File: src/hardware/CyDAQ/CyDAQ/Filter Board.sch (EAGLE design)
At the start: 213 parts, among them J1 DCJ0202, J10 Vout_HEADER, J11 5V0_SENSOR, J12 3V3_SENSOR, J13 1V8_SENSOR, J14 BRKOUT_JD, J15 BRKOUT_JC, J16 BRKOUT_JB, J17 BRKOUT_JF, J18 5V0_CONN, J19 3V3_CONN, J2 ZYBO_JF, J20 1V8_CONN, J21 BRKOUT_JD, J22 ZYBO_Power, J3 ZYBO_JE, J4 ZYBO_JD, J5 ZYBO_JC, J6 ZYBO_JB, J7 A_XADC, J8 SJ1-3523N, J9 Vin_HEADER, U1 TPS54531DDARDDA8_3P1X2P4-L, U10 CD74HCT4051, U11 CD74HCT4051, U12 OPA4197, U13 OPA4197, U14 OPA4197, U15 OPA4197, U16 OPA4197, U17 CD74HCT4053, U18 CD74HCT4051, U19 OPA2197, U3 TPS56339, U4 TPS56339, U5 LM43601PWPR, U6 X9258_A, U7 X925_B, U8 X9258_C, U9 X9258_D

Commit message: Made some final adjustments and added production files
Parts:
- added R43: 10k, Resistors:SMD_0805
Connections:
- net 3.5MM_IN: now also J8.2; no longer J8.1
- net GND: now also J8.1, R43.1; no longer J8.2
- net N$73: now also R43.2
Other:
- note removed: "Pull-up/down resistors on U1"
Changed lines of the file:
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@@
 <attribute name="ENGINEER_NAME" value="Samuel Burnett"/>
 </part>
+<part name="R43" library="Resistors" library_urn="urn:adsk.eagle:library:4010572" deviceset="SMD" device="_0805" package3d_urn="urn:adsk.eagle:package:4010580/4" value="10k"/>
+<part name="SUPPLY93" library="supply2" library_urn="urn:adsk.eagle:library:372" deviceset="GND" device=""/>
 </parts>
 <sheets>
@@
 <text x="195.072" y="108.712" size="1.27" layer="97">NC</text>
 <text x="324.612" y="108.712" size="1.27" layer="97">NC</text>
-<text x="10.16" y="40.132" size="1.778" layer="97">Pull-up/down
-resistors on U1</text>
-<text x="294.64" y="114.3" size="1.778" layer="97">Pull-up/down
-resistors on U1</text>
-<text x="170.18" y="114.3" size="1.778" layer="97">Pull-up/down
-resistors on U1</text>
 <text x="93.726" y="128.524" size="1.778" layer="97">Address: 0x0</text>
 <text x="218.186" y="128.524" size="1.778" layer="97">Address: 0x6</text>
@@
 <text x="229.108" y="73.152" size="1.27" layer="97">0.1%</text>
 <text x="244.094" y="73.152" size="1.27" layer="97">0.1%</text>
-<wire x1="152.4" y1="88.9" x2="271.78" y2="88.9" width="0.1524" layer="97" style="longdash"/>
-<wire x1="271.78" y1="88.9" x2="271.78" y2="10.16" width="0.1524" layer="97" style="longdash"/>
-<wire x1="271.78" y1="10.16" x2="152.4" y2="10.16" width="0.1524" layer="97" style="longdash"/>
+<wire x1="152.4" y1="88.9" x2="276.86" y2="88.9" width="0.1524" layer="97" style="longdash"/>
+<wire x1="276.86" y1="88.9" x2="276.86" y2="10.16" width="0.1524" layer="97" style="longdash"/>
+<wire x1="276.86" y1="10.16" x2="152.4" y2="10.16" width="0.1524" layer="97" style="longdash"/>
 <wire x1="152.4" y1="10.16" x2="152.4" y2="88.9" width="0.1524" layer="97" style="longdash"/>
 <text x="154.94" y="71.12" size="5.08" layer="97">Level shifter</text>
@@
 <attribute name="VALUE" x="25.3947" y="128.7727" size="1.778" layer="96"/>
 </instance>
-<instance part="SUPPLY74" gate="GND" x="48.26" y="129.54" smashed="yes"/>
+<instance part="SUPPLY74" gate="GND" x="68.58" y="134.62" smashed="yes"/>
 <instance part="J9" gate="G$1" x="27.94" y="33.02" smashed="yes">
 <attribute name="VALUE" x="25.4" y="28.194" size="1.778" layer="96" font="vector"/>
@@
 <attribute name="ENGINEER_NAME" x="346.71" y="19.05" size="2.54" layer="94"/>
 </instance>
+<instance part="R43" gate="G$1" x="271.78" y="55.88" smashed="yes" rot="R90">
+<attribute name="NAME" x="270.8656" y="60.579" size="1.778" layer="95" rot="R180"/>
+<attribute name="VALUE" x="270.891" y="52.197" size="1.778" layer="96" rot="R180"/>
+</instance>
+<instance part="SUPPLY93" gate="GND" x="271.78" y="45.72" smashed="yes"/>
 </instances>
 <busses>
@@
 </segment>
 <segment>
-<pinref part="J8" gate="G$1" pin="2"/>
-<wire x1="43.18" y1="134.62" x2="48.26" y2="134.62" width="0.1524" layer="91"/>
-<wire x1="48.26" y1="134.62" x2="48.26" y2="132.08" width="0.1524" layer="91"/>
-<pinref part="SUPPLY74" gate="GND" pin="GND"/>
-</segment>
-<segment>
 <pinref part="J9" gate="G$1" pin="1"/>
 <wire x1="35.56" y1="33.02" x2="43.18" y2="33.02" width="0.1524" layer="91"/>
@@
 <pinref part="SUPPLY9" gate="GND" pin="GND"/>
 </segment>
+<segment>
+<pinref part="J8" gate="G$1" pin="1"/>
+<pinref part="SUPPLY74" gate="GND" pin="GND"/>
+<wire x1="43.18" y1="139.7" x2="68.58" y2="139.7" width="0.1524" layer="91"/>
+<wire x1="68.58" y1="139.7" x2="68.58" y2="137.16" width="0.1524" layer="91"/>
+</segment>
+<segment>
+<pinref part="R43" gate="G$1" pin="1"/>
+<pinref part="SUPPLY93" gate="GND" pin="GND"/>
+<wire x1="271.78" y1="50.8" x2="271.78" y2="48.26" width="0.1524" layer="91"/>
+</segment>
 </net>
 <net name="3.5MM_IN" class="0">
 <segment>
-<pinref part="J8" gate="G$1" pin="1"/>
-<wire x1="43.18" y1="139.7" x2="48.26" y2="139.7" width="0.1524" layer="91"/>
-<label x="62.738" y="139.7" size="1.27" layer="95" rot="R180" xref="yes"/>
+<pinref part="J8" gate="G$1" pin="2"/>
+<wire x1="43.18" y1="134.62" x2="48.26" y2="134.62" width="0.1524" layer="91"/>
+<label x="62.738" y="134.62" size="1.27" layer="95" rot="R180" xref="yes"/>
 </segment>
 </net>
@@
 <wire x1="299.72" y1="73.66" x2="302.26" y2="73.66" width="0.1524" layer="91"/>
 <wire x1="302.26" y1="73.66" x2="302.26" y2="66.04" width="0.1524" layer="91"/>
-<wire x1="302.26" y1="66.04" x2="264.16" y2="66.04" width="0.1524" layer="91"/>
+<wire x1="302.26" y1="66.04" x2="271.78" y2="66.04" width="0.1524" layer="91"/>
 <junction x="264.16" y="66.04"/>
+<pinref part="R43" gate="G$1" pin="2"/>
+<wire x1="271.78" y1="66.04" x2="264.16" y2="66.04" width="0.1524" layer="91"/>
+<wire x1="271.78" y1="60.96" x2="271.78" y2="66.04" width="0.1524" layer="91"/>
+<junction x="271.78" y="66.04"/>
 </segment>
 </net>

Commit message: Adjusted notch filter values and uploaded BOM
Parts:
- C31: value 10uF -> 0.1uF
- C34, C35: value 5.6uF -> 0.1uF
- R39, R40: value 470 -> 39k
- R46: value 220 -> 9.1k
- R60, R65: value 50k -> 51k
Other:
- note added: "Center Frequency = 59Hz"
- note removed: "Center Frequency = 64Hz"
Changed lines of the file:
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@@
 <part name="U10" library="Digital ICs" library_urn="urn:adsk.eagle:library:14993291" deviceset="CD74HCT4051" device="" package3d_urn="urn:adsk.eagle:package:14993294/2" value="CD74HCT4051"/>
 <part name="U11" library="Digital ICs" library_urn="urn:adsk.eagle:library:14993291" deviceset="CD74HCT4051" device="" package3d_urn="urn:adsk.eagle:package:14993294/2" value="CD74HCT4051"/>
-<part name="R39" library="Resistors" library_urn="urn:adsk.eagle:library:4010572" deviceset="SMD" device="_0805" package3d_urn="urn:adsk.eagle:package:4010580/4" value="470"/>
-<part name="R40" library="Resistors" library_urn="urn:adsk.eagle:library:4010572" deviceset="SMD" device="_0805" package3d_urn="urn:adsk.eagle:package:4010580/4" value="470"/>
-<part name="R46" library="Resistors" library_urn="urn:adsk.eagle:library:4010572" deviceset="SMD" device="_0805" package3d_urn="urn:adsk.eagle:package:4010580/4" value="220"/>
-<part name="C35" library="Capacitors" library_urn="urn:adsk.eagle:library:4010381" deviceset="NON_POL" device="_0805/2012" package3d_urn="urn:adsk.eagle:package:4010399/3" value="5.6uF"/>
-<part name="C34" library="Capacitors" library_urn="urn:adsk.eagle:library:4010381" deviceset="NON_POL" device="_0805/2012" package3d_urn="urn:adsk.eagle:package:4010399/3" value="5.6uF"/>
-<part name="C31" library="Capacitors" library_urn="urn:adsk.eagle:library:4010381" deviceset="NON_POL" device="_0805/2012" package3d_urn="urn:adsk.eagle:package:4010399/3" value="10uF"/>
+<part name="R39" library="Resistors" library_urn="urn:adsk.eagle:library:4010572" deviceset="SMD" device="_0805" package3d_urn="urn:adsk.eagle:package:4010580/4" value="39k"/>
+<part name="R40" library="Resistors" library_urn="urn:adsk.eagle:library:4010572" deviceset="SMD" device="_0805" package3d_urn="urn:adsk.eagle:package:4010580/4" value="39k"/>
+<part name="R46" library="Resistors" library_urn="urn:adsk.eagle:library:4010572" deviceset="SMD" device="_0805" package3d_urn="urn:adsk.eagle:package:4010580/4" value="9.1k"/>
+<part name="C35" library="Capacitors" library_urn="urn:adsk.eagle:library:4010381" deviceset="NON_POL" device="_0805/2012" package3d_urn="urn:adsk.eagle:package:4010399/3" value="0.1uF"/>
+<part name="C34" library="Capacitors" library_urn="urn:adsk.eagle:library:4010381" deviceset="NON_POL" device="_0805/2012" package3d_urn="urn:adsk.eagle:package:4010399/3" value="0.1uF"/>
+<part name="C31" library="Capacitors" library_urn="urn:adsk.eagle:library:4010381" deviceset="NON_POL" device="_0805/2012" package3d_urn="urn:adsk.eagle:package:4010399/3" value="0.1uF"/>
 <part name="SUPPLY44" library="supply2" library_urn="urn:adsk.eagle:library:372" deviceset="GND" device=""/>
 <part name="SUPPLY49" library="supply2" library_urn="urn:adsk.eagle:library:372" deviceset="GND" device=""/>
@@
 <part name="R58" library="Resistors" library_urn="urn:adsk.eagle:library:4010572" deviceset="SMD" device="_0805" package3d_urn="urn:adsk.eagle:package:4010580/4" value="100k"/>
 <part name="R59" library="Resistors" library_urn="urn:adsk.eagle:library:4010572" deviceset="SMD" device="_0805" package3d_urn="urn:adsk.eagle:package:4010580/4" value="100k"/>
-<part name="R60" library="Resistors" library_urn="urn:adsk.eagle:library:4010572" deviceset="SMD" device="_0805" package3d_urn="urn:adsk.eagle:package:4010580/4" value="50k"/>
+<part name="R60" library="Resistors" library_urn="urn:adsk.eagle:library:4010572" deviceset="SMD" device="_0805" package3d_urn="urn:adsk.eagle:package:4010580/4" value="51k"/>
 <part name="SUPPLY63" library="supply2" library_urn="urn:adsk.eagle:library:372" deviceset="GND" device=""/>
 <part name="R61" library="Resistors" library_urn="urn:adsk.eagle:library:4010572" deviceset="SMD" device="_0805" package3d_urn="urn:adsk.eagle:package:4010580/4" value="100k"/>
@@
 <part name="R63" library="Resistors" library_urn="urn:adsk.eagle:library:4010572" deviceset="SMD" device="_0805" package3d_urn="urn:adsk.eagle:package:4010580/4" value="100k"/>
 <part name="R64" library="Resistors" library_urn="urn:adsk.eagle:library:4010572" deviceset="SMD" device="_0805" package3d_urn="urn:adsk.eagle:package:4010580/4" value="100k"/>
-<part name="R65" library="Resistors" library_urn="urn:adsk.eagle:library:4010572" deviceset="SMD" device="_0805" package3d_urn="urn:adsk.eagle:package:4010580/4" value="50k"/>
+<part name="R65" library="Resistors" library_urn="urn:adsk.eagle:library:4010572" deviceset="SMD" device="_0805" package3d_urn="urn:adsk.eagle:package:4010580/4" value="51k"/>
 <part name="R66" library="Resistors" library_urn="urn:adsk.eagle:library:4010572" deviceset="SMD" device="_0805" package3d_urn="urn:adsk.eagle:package:4010580/4" value="100k"/>
 <part name="SUPPLY66" library="supply2" library_urn="urn:adsk.eagle:library:372" deviceset="GND" device=""/>
@@
 &lt;/ul&gt;</description>
 <plain>
-<text x="332.74" y="234.95" size="1.778" layer="97">Center Frequency = 64Hz</text>
+<text x="332.74" y="234.95" size="1.778" layer="97">Center Frequency = 59Hz</text>
 <text x="287.02" y="243.84" size="5.08" layer="97">Notch Filter</text>
 <text x="294.64" y="104.14" size="5.08" layer="97">1st Order High Pass</text>

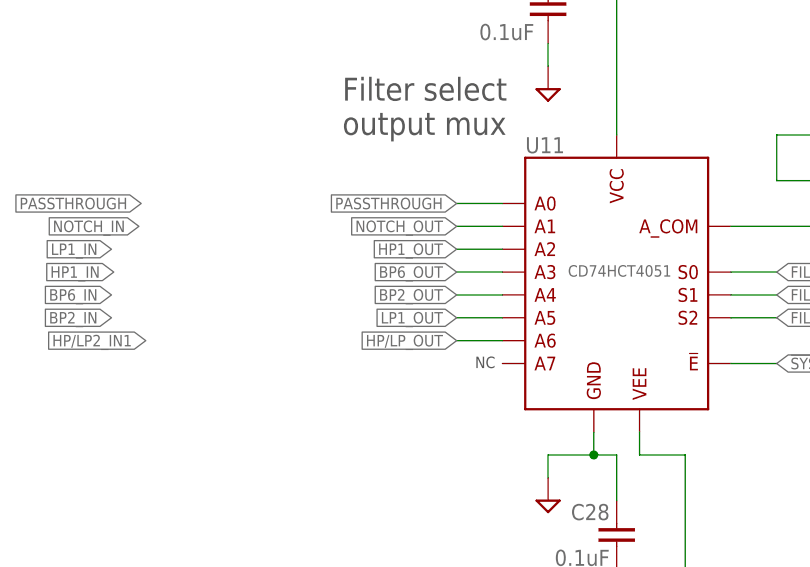
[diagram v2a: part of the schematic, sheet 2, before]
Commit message: Fixed output MUX mapping
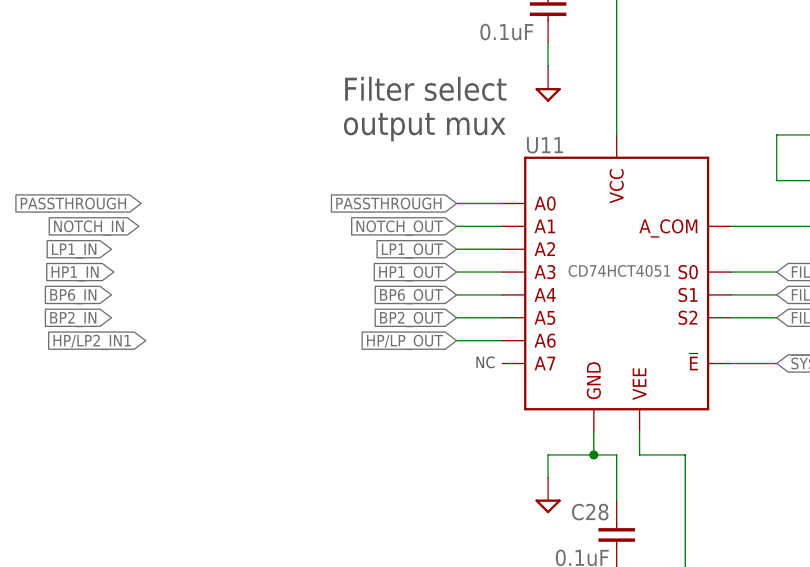
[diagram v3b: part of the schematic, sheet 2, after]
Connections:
- net BP2_OUT: now also U11.A5; no longer U11.A4
- net BP6_OUT: now also U11.A4; no longer U11.A3
- net HP1_OUT: now also U11.A3; no longer U11.A2
- net LP1_OUT: now also U11.A2; no longer U11.A5
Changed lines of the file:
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@@
-</segment>
-</net>
-<net name="HP1_OUT" class="0">
-<segment>
-<pinref part="U11" gate="G$1" pin="A2"/>
-<wire x1="218.44" y1="226.06" x2="213.36" y2="226.06" width="0.1524" layer="91"/>
-<label x="213.36" y="226.06" size="1.27" layer="95" rot="R180" xref="yes"/>
-</segment>
-</net>
-<net name="BP2_OUT" class="0">
-<segment>
-<pinref part="U11" gate="G$1" pin="A4"/>
-<wire x1="218.44" y1="220.98" x2="213.36" y2="220.98" width="0.1524" layer="91"/>
-<label x="213.36" y="220.98" size="1.27" layer="95" rot="R180" xref="yes"/>
-</segment>
-</net>
-<net name="BP6_OUT" class="0">
-<segment>
-<pinref part="U11" gate="G$1" pin="A3"/>
-<wire x1="218.44" y1="223.52" x2="213.36" y2="223.52" width="0.1524" layer="91"/>
-<label x="213.36" y="223.52" size="1.27" layer="95" rot="R180" xref="yes"/>
 </segment>
 </net>
@@
 <net name="LP1_OUT" class="0">
 <segment>
+<pinref part="U11" gate="G$1" pin="A2"/>
+<wire x1="218.44" y1="226.06" x2="213.36" y2="226.06" width="0.1524" layer="91"/>
+<label x="213.36" y="226.06" size="1.27" layer="95" rot="R180" xref="yes"/>
+</segment>
+</net>
+<net name="LP1_IN" class="0">
+<segment>
+<pinref part="U10" gate="G$1" pin="A2"/>
+<wire x1="157.48" y1="226.06" x2="162.56" y2="226.06" width="0.1524" layer="91"/>
+<label x="175.006" y="226.06" size="1.27" layer="95" rot="R180" xref="yes"/>
+</segment>
+</net>
+<net name="HP1_OUT" class="0">
+<segment>
+<pinref part="U11" gate="G$1" pin="A3"/>
+<wire x1="218.44" y1="223.52" x2="213.36" y2="223.52" width="0.1524" layer="91"/>
+<label x="213.36" y="223.52" size="1.27" layer="95" rot="R180" xref="yes"/>
+</segment>
+</net>
+<net name="BP6_OUT" class="0">
+<segment>
+<pinref part="U11" gate="G$1" pin="A4"/>
+<wire x1="218.44" y1="220.98" x2="213.36" y2="220.98" width="0.1524" layer="91"/>
+<label x="213.36" y="220.98" size="1.27" layer="95" rot="R180" xref="yes"/>
+</segment>
+</net>
+<net name="BP2_OUT" class="0">
+<segment>
 <pinref part="U11" gate="G$1" pin="A5"/>
 <wire x1="218.44" y1="218.44" x2="213.36" y2="218.44" width="0.1524" layer="91"/>
@@
 </segment>
 </net>
-<net name="LP1_IN" class="0">
-<segment>
-<pinref part="U10" gate="G$1" pin="A2"/>
-<wire x1="157.48" y1="226.06" x2="162.56" y2="226.06" width="0.1524" layer="91"/>
-<label x="175.006" y="226.06" size="1.27" layer="95" rot="R180" xref="yes"/>
-</segment>
-</net>

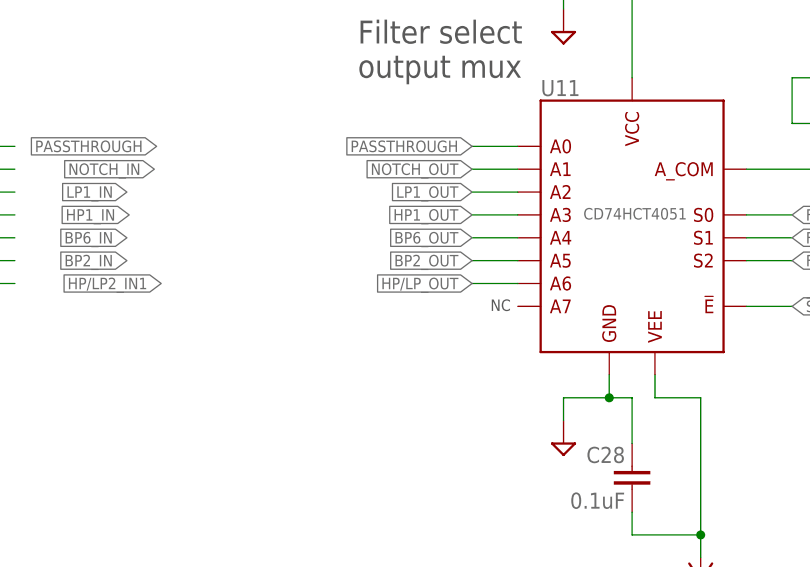
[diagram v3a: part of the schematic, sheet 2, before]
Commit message: Started fixing pinout on MUXs
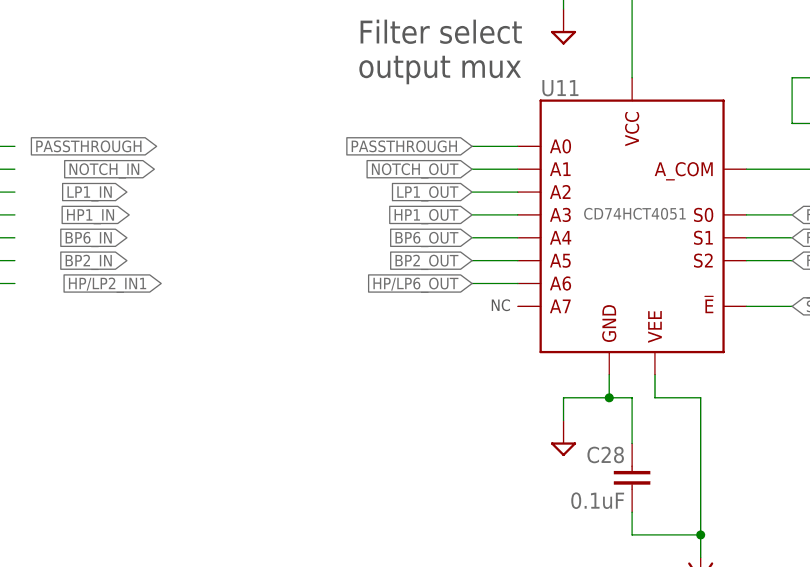
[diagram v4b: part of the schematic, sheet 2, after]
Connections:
- removed net HP/LP_OUT: U11.A6
- net -5V0: now also U10.VEE, U11.VEE, U17.VEE, U18.VEE; no longer U10.GND, U11.GND, U17.GND, U18.GND
- net GND: now also U10.GND, U11.GND, U17.GND, U18.GND; no longer U10.VEE, U11.VEE, U17.VEE, U18.VEE
- net HP/LP6_OUT: now also U11.A6
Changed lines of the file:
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@@
 <drawing>
 <settings>
-<setting alwaysvectorfont="no"/>
+<setting alwaysvectorfont="yes"/>
 <setting verticaltext="up"/>
 </settings>
@@
 <net name="GND" class="2">
 <segment>
-<pinref part="U10" gate="G$1" pin="VEE"/>
+<pinref part="U10" gate="G$1" pin="GND"/>
 <wire x1="147.32" y1="205.74" x2="147.32" y2="203.2" width="0.1524" layer="91"/>
 <wire x1="147.32" y1="203.2" x2="152.4" y2="203.2" width="0.1524" layer="91"/>
@@
 <pinref part="SUPPLY8" gate="GND" pin="GND"/>
 <wire x1="373.38" y1="203.2" x2="373.38" y2="200.66" width="0.1524" layer="91"/>
-<pinref part="U17" gate="G$1" pin="VEE"/>
+<pinref part="U17" gate="G$1" pin="GND"/>
 <pinref part="C29" gate="G$1" pin="1"/>
 <wire x1="381" y1="198.12" x2="381" y2="203.2" width="0.1524" layer="91"/>
@@
 </segment>
 <segment>
-<pinref part="U11" gate="G$1" pin="VEE"/>
+<pinref part="U11" gate="G$1" pin="GND"/>
 <wire x1="228.6" y1="205.74" x2="228.6" y2="203.2" width="0.1524" layer="91"/>
 <wire x1="228.6" y1="203.2" x2="223.52" y2="203.2" width="0.1524" layer="91"/>
@@
 <pinref part="SUPPLY5" gate="GND" pin="GND"/>
 <wire x1="48.26" y1="203.2" x2="48.26" y2="200.66" width="0.1524" layer="91"/>
-<pinref part="U18" gate="G$1" pin="VEE"/>
+<pinref part="U18" gate="G$1" pin="GND"/>
 <wire x1="55.88" y1="203.2" x2="53.34" y2="203.2" width="0.1524" layer="91"/>
 <junction x="53.34" y="203.2"/>
@@
 <wire x1="139.7" y1="187.96" x2="139.7" y2="203.2" width="0.1524" layer="91"/>
 <wire x1="139.7" y1="203.2" x2="142.24" y2="203.2" width="0.1524" layer="91"/>
-<pinref part="U10" gate="G$1" pin="GND"/>
+<pinref part="U10" gate="G$1" pin="VEE"/>
 <wire x1="142.24" y1="203.2" x2="142.24" y2="205.74" width="0.1524" layer="91"/>
 <pinref part="C27" gate="G$1" pin="1"/>
@@
 <wire x1="386.08" y1="203.2" x2="383.54" y2="203.2" width="0.1524" layer="91"/>
 <wire x1="383.54" y1="203.2" x2="383.54" y2="205.74" width="0.1524" layer="91"/>
-<pinref part="U17" gate="G$1" pin="GND"/>
+<pinref part="U17" gate="G$1" pin="VEE"/>
 <pinref part="C29" gate="G$1" pin="2"/>
 <wire x1="381" y1="190.5" x2="381" y2="187.96" width="0.1524" layer="91"/>
@@
 <wire x1="238.76" y1="203.2" x2="233.68" y2="203.2" width="0.1524" layer="91"/>
 <wire x1="233.68" y1="203.2" x2="233.68" y2="205.74" width="0.1524" layer="91"/>
-<pinref part="U11" gate="G$1" pin="GND"/>
+<pinref part="U11" gate="G$1" pin="VEE"/>
 <pinref part="C28" gate="G$1" pin="2"/>
 <wire x1="231.14" y1="190.5" x2="231.14" y2="187.96" width="0.1524" layer="91"/>
@@
 <wire x1="60.96" y1="203.2" x2="58.42" y2="203.2" width="0.1524" layer="91"/>
 <wire x1="58.42" y1="203.2" x2="58.42" y2="205.74" width="0.1524" layer="91"/>
-<pinref part="U18" gate="G$1" pin="GND"/>
+<pinref part="U18" gate="G$1" pin="VEE"/>
 <wire x1="60.96" y1="187.96" x2="55.88" y2="187.96" width="0.1524" layer="91"/>
 <junction x="60.96" y="187.96"/>
@@
 </segment>
 </net>
-<net name="HP/LP_OUT" class="0">
+<net name="HP/LP6_OUT" class="0">
+<segment>
+<pinref part="U17" gate="G$1" pin="C_COM"/>
+<wire x1="393.7" y1="226.06" x2="398.78" y2="226.06" width="0.1524" layer="91"/>
+<label x="411.734" y="226.06" size="1.27" layer="95" rot="R180" xref="yes"/>
+</segment>
 <segment>
 <pinref part="U11" gate="G$1" pin="A6"/>
@@
 </segment>
 </net>
-<net name="HP/LP6_OUT" class="0">
-<segment>
-<pinref part="U17" gate="G$1" pin="C_COM"/>
-<wire x1="393.7" y1="226.06" x2="398.78" y2="226.06" width="0.1524" layer="91"/>
-<label x="411.734" y="226.06" size="1.27" layer="95" rot="R180" xref="yes"/>
-</segment>
-</net>
